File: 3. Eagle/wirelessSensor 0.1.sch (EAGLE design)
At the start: 15 parts, among them U1 HDC1080, U2 PIC16F1823-X_SL, X1 22-23-2021

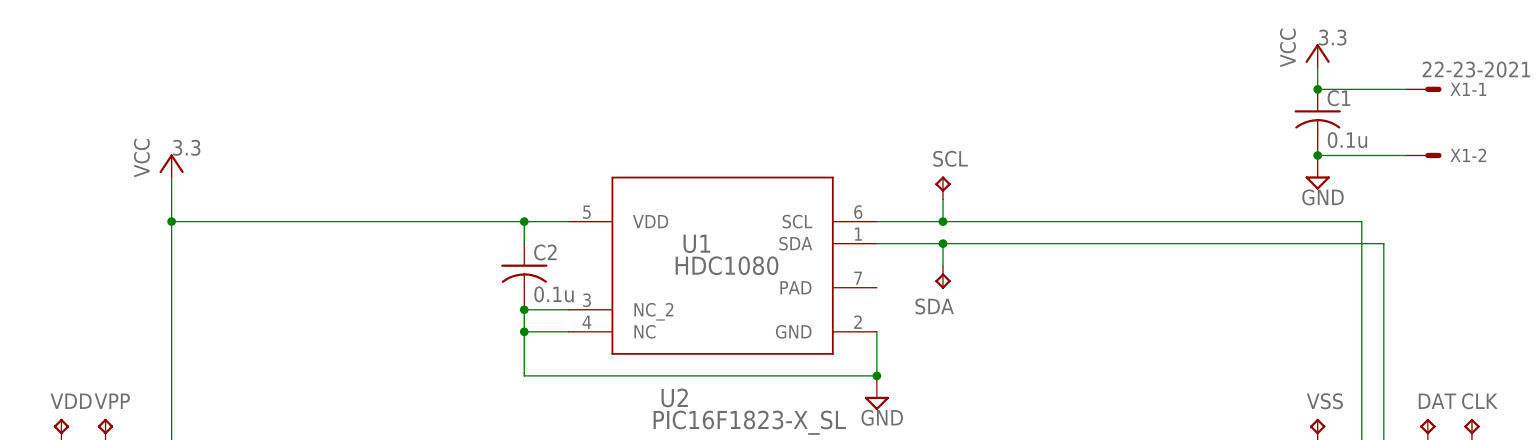
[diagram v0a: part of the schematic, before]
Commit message: Started work on the I2C interface, and organized the code a bit more
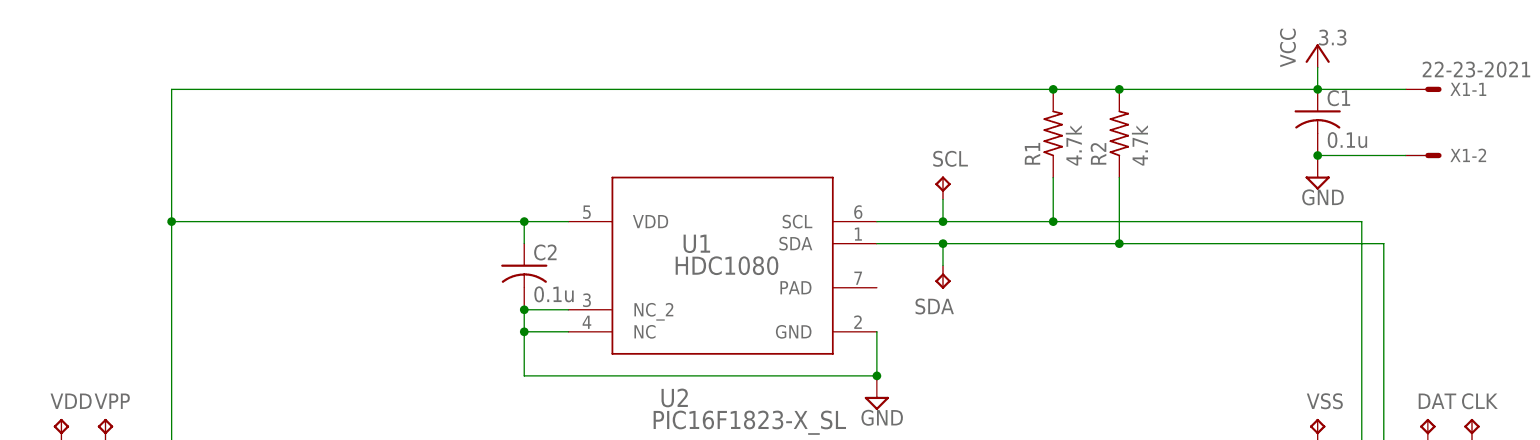
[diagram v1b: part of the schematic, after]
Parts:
- added R1, R2: 4.7k, rcl:R-US_R0603
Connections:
- net N$2: now also R1.1
- net N$3: now also R2.1
- net VCC: now also R1.2, R2.2
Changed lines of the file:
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@@
 <part name="U1" library="wirelessSensor" deviceset="HDC1080DMBR" device="" value="HDC1080"/>
 <part name="U2" library="wirelessSensor" deviceset="PIC16F1823-X_SL" device=""/>
-<part name="+3.3" library="supply1" deviceset="VCC" device="">
-<attribute name="VOLTAGE" value="3.3"/>
-</part>
 <part name="SUPPLY1" library="supply2" deviceset="GND" device=""/>
 <part name="SUPPLY2" library="supply2" deviceset="GND" device=""/>
@@
 <part name="RX" library="testpad" deviceset="TP" device="B1,27"/>
 <part name="TX" library="testpad" deviceset="TP" device="B1,27"/>
+<part name="R1" library="rcl" deviceset="R-US_" device="R0603" value="4.7k"/>
+<part name="R2" library="rcl" deviceset="R-US_" device="R0603" value="4.7k"/>
 </parts>
 <sheets>
@@
 <instance part="U1" gate="A" x="0" y="27.94"/>
 <instance part="U2" gate="A" x="0" y="-5.08"/>
-<instance part="+3.3" gate="VCC" x="-63.5" y="40.64">
-<attribute name="VOLTAGE" x="-63.5" y="40.64" size="1.778" layer="96"/>
-</instance>
 <instance part="SUPPLY1" gate="GND" x="68.58" y="-20.32"/>
 <instance part="SUPPLY2" gate="GND" x="17.78" y="12.7"/>
@@
 <instance part="RX" gate="G$1" x="-76.2" y="-17.78"/>
 <instance part="TX" gate="G$1" x="-66.04" y="-17.78"/>
+<instance part="R1" gate="G$1" x="38.1" y="43.18" rot="R90"/>
+<instance part="R2" gate="G$1" x="45.72" y="43.18" rot="R90"/>
 </instances>
 <busses>
@@
 <net name="VCC" class="0">
 <segment>
+<pinref part="+3.1" gate="VCC" pin="VCC"/>
+<pinref part="C1" gate="G$1" pin="1"/>
+<wire x1="68.58" y1="50.8" x2="68.58" y2="48.26" width="0.1524" layer="91"/>
+<pinref part="X1" gate="-1" pin="S"/>
+<wire x1="78.74" y1="48.26" x2="68.58" y2="48.26" width="0.1524" layer="91"/>
+<junction x="68.58" y="48.26"/>
+<pinref part="R2" gate="G$1" pin="2"/>
+<wire x1="45.72" y1="48.26" x2="68.58" y2="48.26" width="0.1524" layer="91"/>
+<pinref part="R1" gate="G$1" pin="2"/>
+<wire x1="38.1" y1="48.26" x2="45.72" y2="48.26" width="0.1524" layer="91"/>
+<junction x="45.72" y="48.26"/>
 <pinref part="U2" gate="A" pin="VDD"/>
 <wire x1="-63.5" y1="2.54" x2="-63.5" y2="33.02" width="0.1524" layer="91"/>
 <pinref part="U1" gate="A" pin="VDD"/>
 <wire x1="-63.5" y1="33.02" x2="-22.86" y2="33.02" width="0.1524" layer="91"/>
-<pinref part="+3.3" gate="VCC" pin="VCC"/>
 <wire x1="-22.86" y1="33.02" x2="-17.78" y2="33.02" width="0.1524" layer="91"/>
-<wire x1="-63.5" y1="38.1" x2="-63.5" y2="33.02" width="0.1524" layer="91"/>
-<junction x="-63.5" y="33.02"/>
 <wire x1="-63.5" y1="2.54" x2="-76.2" y2="2.54" width="0.1524" layer="91"/>
 <junction x="-63.5" y="2.54"/>
@@
 <wire x1="-22.86" y1="33.02" x2="-22.86" y2="30.48" width="0.1524" layer="91"/>
 <junction x="-22.86" y="33.02"/>
-</segment>
-<segment>
-<pinref part="+3.1" gate="VCC" pin="VCC"/>
-<pinref part="C1" gate="G$1" pin="1"/>
-<wire x1="68.58" y1="50.8" x2="68.58" y2="48.26" width="0.1524" layer="91"/>
-<pinref part="X1" gate="-1" pin="S"/>
-<wire x1="78.74" y1="48.26" x2="68.58" y2="48.26" width="0.1524" layer="91"/>
-<junction x="68.58" y="48.26"/>
+<wire x1="-63.5" y1="33.02" x2="-63.5" y2="48.26" width="0.1524" layer="91"/>
+<junction x="-63.5" y="33.02"/>
+<wire x1="-63.5" y1="48.26" x2="38.1" y2="48.26" width="0.1524" layer="91"/>
+<junction x="38.1" y="48.26"/>
 </segment>
 <segment>
@@
 <wire x1="73.66" y1="-7.62" x2="73.66" y2="33.02" width="0.1524" layer="91"/>
 <pinref part="U1" gate="A" pin="SCL"/>
-<wire x1="73.66" y1="33.02" x2="25.4" y2="33.02" width="0.1524" layer="91"/>
+<wire x1="73.66" y1="33.02" x2="38.1" y2="33.02" width="0.1524" layer="91"/>
 <pinref part="SCL" gate="G$1" pin="TP"/>
+<wire x1="38.1" y1="33.02" x2="25.4" y2="33.02" width="0.1524" layer="91"/>
 <wire x1="25.4" y1="33.02" x2="17.78" y2="33.02" width="0.1524" layer="91"/>
 <wire x1="25.4" y1="35.56" x2="25.4" y2="33.02" width="0.1524" layer="91"/>
 <junction x="25.4" y="33.02"/>
+<pinref part="R1" gate="G$1" pin="1"/>
+<wire x1="38.1" y1="38.1" x2="38.1" y2="33.02" width="0.1524" layer="91"/>
+<junction x="38.1" y="33.02"/>
 </segment>
 </net>
@@
 <wire x1="76.2" y1="-10.16" x2="76.2" y2="30.48" width="0.1524" layer="91"/>
 <pinref part="U1" gate="A" pin="SDA"/>
-<wire x1="76.2" y1="30.48" x2="25.4" y2="30.48" width="0.1524" layer="91"/>
+<wire x1="76.2" y1="30.48" x2="45.72" y2="30.48" width="0.1524" layer="91"/>
 <pinref part="SDA" gate="G$1" pin="TP"/>
+<wire x1="45.72" y1="30.48" x2="25.4" y2="30.48" width="0.1524" layer="91"/>
 <wire x1="25.4" y1="30.48" x2="17.78" y2="30.48" width="0.1524" layer="91"/>
 <wire x1="25.4" y1="27.94" x2="25.4" y2="30.48" width="0.1524" layer="91"/>
 <junction x="25.4" y="30.48"/>
+<pinref part="R2" gate="G$1" pin="1"/>
+<wire x1="45.72" y1="38.1" x2="45.72" y2="30.48" width="0.1524" layer="91"/>
+<junction x="45.72" y="30.48"/>
 </segment>
 </net>
